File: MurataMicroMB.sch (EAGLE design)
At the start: 54 parts, among them CON1 C-2395, CON2 WM17143CT-ND, CON3 CON_MIL_10_ARM, CON4 C-2395, IC1 NC7SZ00M5XCT-ND, IC2 296-35164-1-ND, IC3 IC_LPC11U3XQFN33, IC4 AZ1117EH-3.3TRG1DICT-ND, Q1 1253-1168-1-ND, SW1 P-8073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

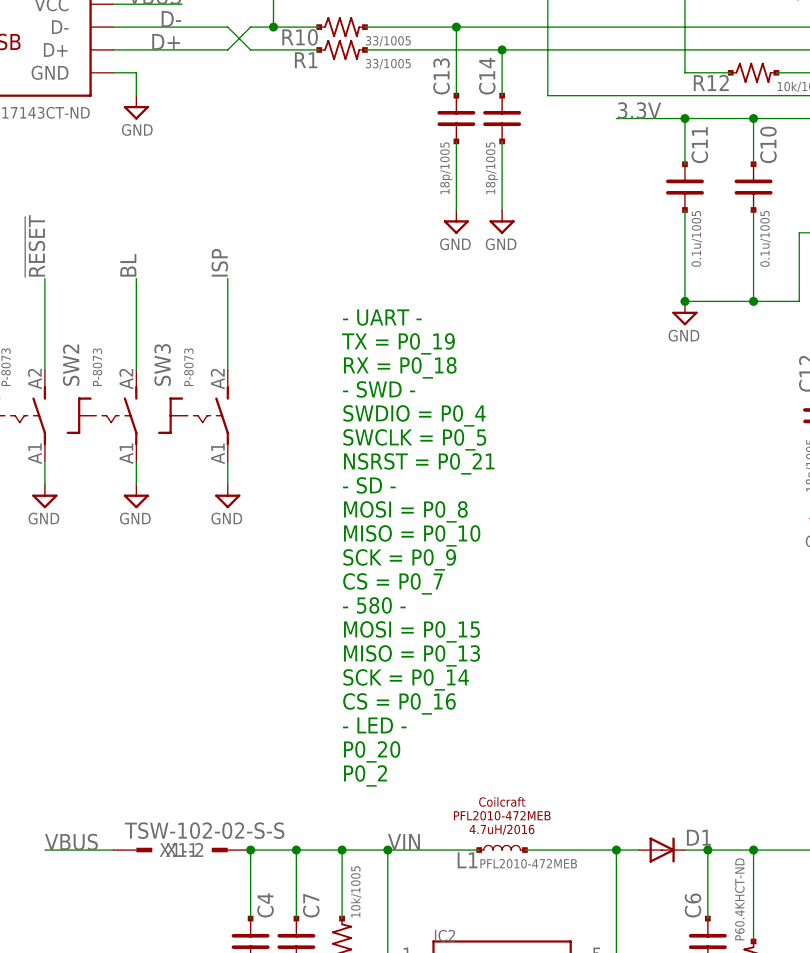
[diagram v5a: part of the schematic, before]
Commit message: [ MB ] R5/6/15/16 moved; add DETECT1/2 pin on schematic
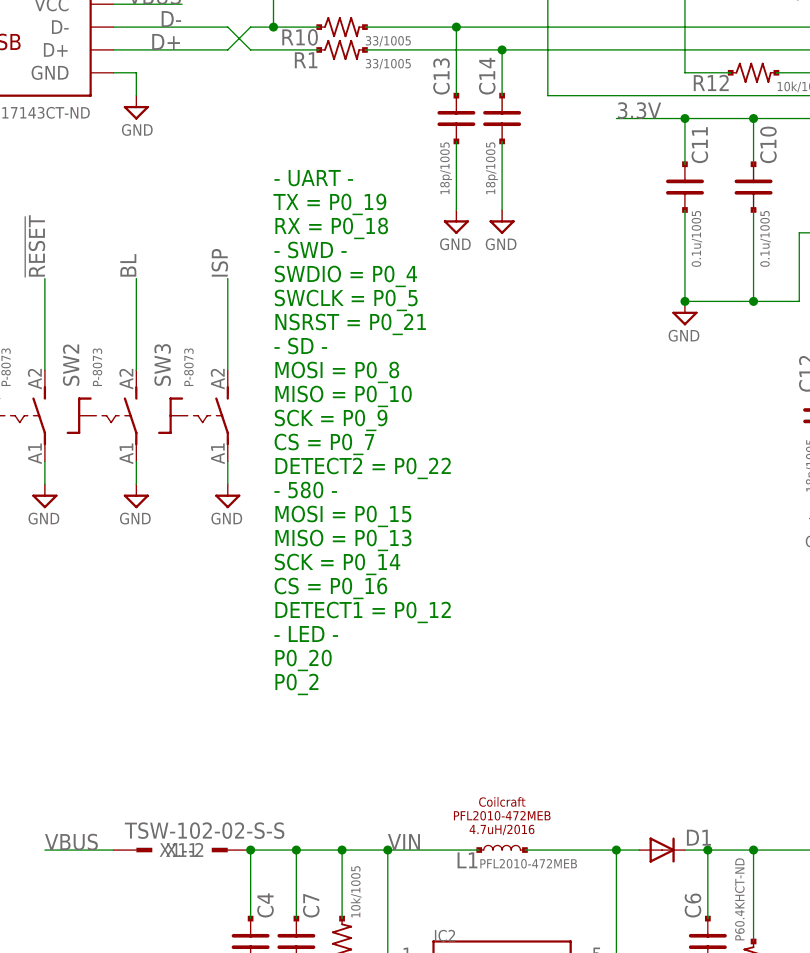
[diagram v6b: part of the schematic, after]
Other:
- note added: "- UART - TX = P0_19 RX = P0_18 - SWD - SWDIO = P0_4 SWCLK = P0_5 NSRST = P0_21 - SD - MOSI = P0_8 MISO = P0_10 SCK = P0_9 CS = P0_7 DETECT2 = P0_22 - 580 - MOSI = P0_15 MISO = P0_13 SCK = P0_14 CS = P0_16 DETECT1 = P0_12 - LED - P0_20 P0_2"
- note removed: "- UART - TX = P0_19 RX = P0_18 - SWD - SWDIO = P0_4 SWCLK = P0_5 NSRST = P0_21 - SD - MOSI = P0_8 MISO = P0_10 SCK = P0_9 CS = P0_7 - 580 - MOSI = P0_15 MISO = P0_13 SCK = P0_14 CS = P0_16 - LED - P0_20 P0_2"
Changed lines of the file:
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@@
 <text x="243.84" y="73.66" size="1.27" layer="94" rot="R90" align="center">MurataMicroSD</text>
 <text x="243.84" y="147.32" size="1.27" layer="94" rot="R90" align="center">microSD</text>
-<text x="55.88" y="53.34" size="1.778" layer="91">- UART -
+<text x="48.26" y="63.5" size="1.778" layer="91">- UART -
 TX = P0_19
 RX = P0_18
@@
 SCK = P0_9
 CS = P0_7
+DETECT2 = P0_22
 - 580 -
 MOSI = P0_15
@@
 SCK = P0_14
 CS = P0_16
+DETECT1 = P0_12
 - LED -
 P0_20

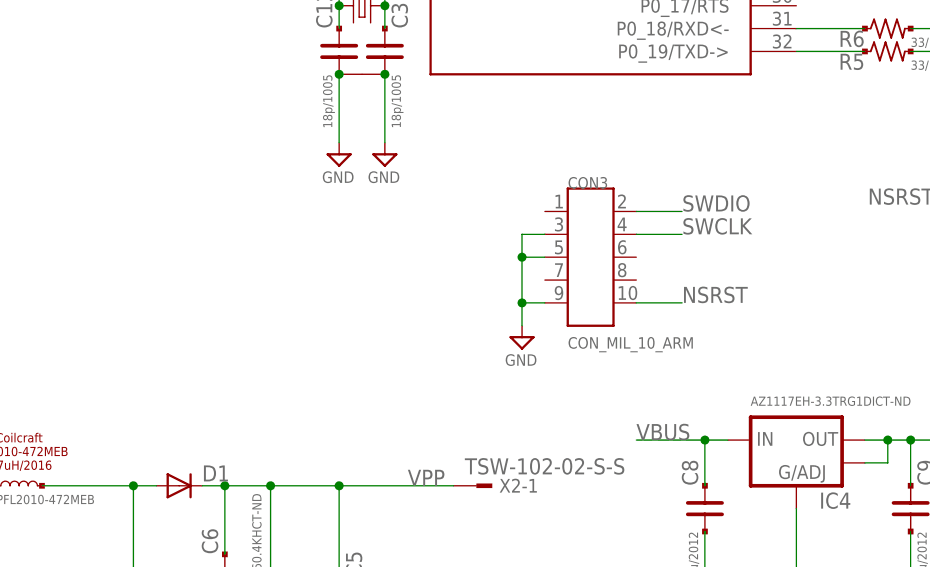
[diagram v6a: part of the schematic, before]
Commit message: [ MB ] add R17-19
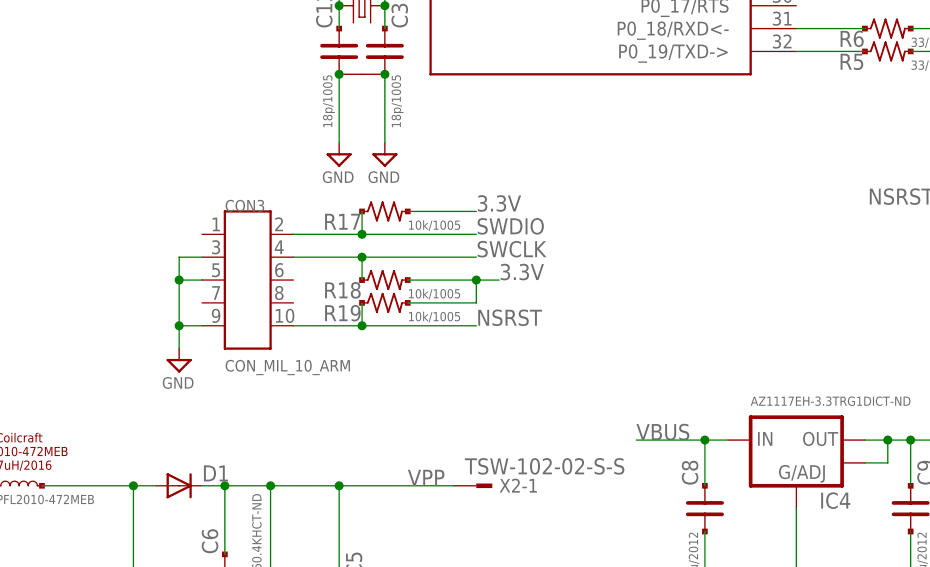
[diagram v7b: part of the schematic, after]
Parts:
- added R17, R18, R19: 10k/1005, mylib:R_US_PAD_PAD_1005
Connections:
- net 3.3V: now also R17.2, R18.2, R19.2
- net NSRST: now also R19.1
- net SWCLK: now also R18.1
- net SWDIO: now also R17.1
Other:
- moved on the sheet: CON3
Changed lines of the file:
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@@
 <part name="TP5" library="mylib" deviceset="TESTPAD" device="_F"/>
 <part name="X2" library="con-samtec.local" deviceset="TSW-102-02-S-S" device=""/>
+<part name="R17" library="mylib" deviceset="R_US_PAD_PAD" device="_1005" value="10k/1005"/>
+<part name="R18" library="mylib" deviceset="R_US_PAD_PAD" device="_1005" value="10k/1005"/>
+<part name="R19" library="mylib" deviceset="R_US_PAD_PAD" device="_1005" value="10k/1005"/>
 </parts>
 <sheets>
@@
 <instance part="IC1" gate="P" x="193.04" y="78.74"/>
 <instance part="CON2" gate="G$1" x="20.32" y="134.62" rot="MR0"/>
-<instance part="CON3" gate="G$1" x="137.16" y="71.12"/>
+<instance part="CON3" gate="G$1" x="99.06" y="68.58"/>
 <instance part="SUPPLY1" gate="GND" x="33.02" y="127" rot="MR0"/>
-<instance part="SUPPLY5" gate="GND" x="129.54" y="60.96"/>
+<instance part="SUPPLY5" gate="GND" x="91.44" y="58.42"/>
 <instance part="SUPPLY3" gate="GND" x="193.04" y="66.04"/>
 <instance part="SUPPLY4" gate="GND" x="223.52" y="53.34" rot="R270"/>
@@
 <instance part="X2" gate="-1" x="124.46" y="45.72"/>
 <instance part="X2" gate="-2" x="124.46" y="12.7"/>
+<instance part="R17" gate="G$1" x="114.3" y="76.2"/>
+<instance part="R18" gate="G$1" x="114.3" y="68.58"/>
+<instance part="R19" gate="G$1" x="114.3" y="66.04"/>
 </instances>
 <busses>
@@
 <segment>
 <pinref part="CON3" gate="G$1" pin="9"/>
-<wire x1="132.08" y1="66.04" x2="129.54" y2="66.04" width="0.1524" layer="91"/>
+<wire x1="93.98" y1="63.5" x2="91.44" y2="63.5" width="0.1524" layer="91"/>
 <pinref part="SUPPLY5" gate="GND" pin="GND"/>
-<wire x1="129.54" y1="66.04" x2="129.54" y2="63.5" width="0.1524" layer="91"/>
+<wire x1="91.44" y1="63.5" x2="91.44" y2="60.96" width="0.1524" layer="91"/>
 <pinref part="CON3" gate="G$1" pin="5"/>
-<wire x1="132.08" y1="71.12" x2="129.54" y2="71.12" width="0.1524" layer="91"/>
-<wire x1="129.54" y1="71.12" x2="129.54" y2="66.04" width="0.1524" layer="91"/>
-<junction x="129.54" y="66.04"/>
+<wire x1="93.98" y1="68.58" x2="91.44" y2="68.58" width="0.1524" layer="91"/>
+<wire x1="91.44" y1="68.58" x2="91.44" y2="63.5" width="0.1524" layer="91"/>
+<junction x="91.44" y="63.5"/>
 <pinref part="CON3" gate="G$1" pin="3"/>
-<wire x1="132.08" y1="73.66" x2="129.54" y2="73.66" width="0.1524" layer="91"/>
-<wire x1="129.54" y1="73.66" x2="129.54" y2="71.12" width="0.1524" layer="91"/>
-<junction x="129.54" y="71.12"/>
+<wire x1="93.98" y1="71.12" x2="91.44" y2="71.12" width="0.1524" layer="91"/>
+<wire x1="91.44" y1="71.12" x2="91.44" y2="68.58" width="0.1524" layer="91"/>
+<junction x="91.44" y="68.58"/>
 </segment>
 <segment>
@@
 <net name="SWCLK" class="0">
 <segment>
-<wire x1="142.24" y1="73.66" x2="147.32" y2="73.66" width="0.1524" layer="91"/>
+<wire x1="104.14" y1="71.12" x2="111.76" y2="71.12" width="0.1524" layer="91"/>
 <pinref part="CON3" gate="G$1" pin="4"/>
-<label x="147.32" y="73.66" size="1.778" layer="95"/>
+<label x="124.46" y="71.12" size="1.778" layer="95"/>
+<pinref part="R18" gate="G$1" pin="1"/>
+<wire x1="111.76" y1="71.12" x2="124.46" y2="71.12" width="0.1524" layer="91"/>
+<wire x1="111.76" y1="68.58" x2="111.76" y2="71.12" width="0.1524" layer="91"/>
+<junction x="111.76" y="71.12"/>
 </segment>
 <segment>
@@
 <net name="SWDIO" class="0">
 <segment>
-<wire x1="142.24" y1="76.2" x2="147.32" y2="76.2" width="0.1524" layer="91"/>
+<wire x1="104.14" y1="73.66" x2="111.76" y2="73.66" width="0.1524" layer="91"/>
 <pinref part="CON3" gate="G$1" pin="2"/>
-<label x="147.32" y="76.2" size="1.778" layer="95"/>
+<label x="124.46" y="73.66" size="1.778" layer="95"/>
+<pinref part="R17" gate="G$1" pin="1"/>
+<wire x1="111.76" y1="73.66" x2="124.46" y2="73.66" width="0.1524" layer="91"/>
+<wire x1="111.76" y1="73.66" x2="111.76" y2="76.2" width="0.1524" layer="91"/>
+<junction x="111.76" y="73.66"/>
 </segment>
 <segment>
@@
 <net name="NSRST" class="0">
 <segment>
-<wire x1="142.24" y1="66.04" x2="147.32" y2="66.04" width="0.1524" layer="91"/>
+<wire x1="104.14" y1="63.5" x2="111.76" y2="63.5" width="0.1524" layer="91"/>
 <pinref part="CON3" gate="G$1" pin="10"/>
-<label x="147.32" y="66.04" size="1.778" layer="95"/>
+<label x="124.46" y="63.5" size="1.778" layer="95"/>
+<pinref part="R19" gate="G$1" pin="1"/>
+<wire x1="111.76" y1="63.5" x2="124.46" y2="63.5" width="0.1524" layer="91"/>
+<wire x1="111.76" y1="66.04" x2="111.76" y2="63.5" width="0.1524" layer="91"/>
+<junction x="111.76" y="63.5"/>
 </segment>
 <segment>
@@
 <junction x="213.36" y="134.62"/>
 </segment>
-</net>
+<segment>
+<wire x1="124.46" y1="76.2" x2="116.84" y2="76.2" width="0.1524" layer="91"/>
+<pinref part="R17" gate="G$1" pin="2"/>
+<label x="124.46" y="76.2" size="1.778" layer="95"/>
+</segment>
+<segment>
+<wire x1="124.46" y1="66.04" x2="116.84" y2="66.04" width="0.1524" layer="91"/>
+<pinref part="R19" gate="G$1" pin="2"/>
+<wire x1="124.46" y1="68.58" x2="116.84" y2="68.58" width="0.1524" layer="91"/>
+<pinref part="R18" gate="G$1" pin="2"/>
+<wire x1="124.46" y1="66.04" x2="124.46" y2="68.58" width="0.1524" layer="91"/>
+<wire x1="124.46" y1="68.58" x2="127" y2="68.58" width="0.1524" layer="91"/>
+<junction x="124.46" y="68.58"/>
+<label x="127" y="68.58" size="1.778" layer="95"/>
+</segment>
+</net>
